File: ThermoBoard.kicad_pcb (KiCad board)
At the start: 4 copper layers, 66 x 75 mm, 153 parts, among them J100 Conn_01x05_Pin, J101 Conn_01x03, J102 TC2030, J103 Screw_Terminal_01x02, J104 USB_C_Receptacle_USB2.0_16P, J200 RJ45_Hanrun_HR911105A_Horizon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, J300 Conn_01x02_Pin, J301 Conn_01x02_Pin, J302 Conn_01x02_Pin, J303 Conn_01x02_Pin, J400 Conn_01x04_Pin, SW100 SW_Push, U100 STM32H563RITx, U101 AP2112K-3.3, U102 USBLC6-2SC6, U200 LAN8742A, U201 USBLC6-4SC6, U300 MAX31856, U301 MAX31856, U302 MAX31856, U303 MAX31856, U400 TJA1042T-3, Y100 16MHz, Y200 25MHz

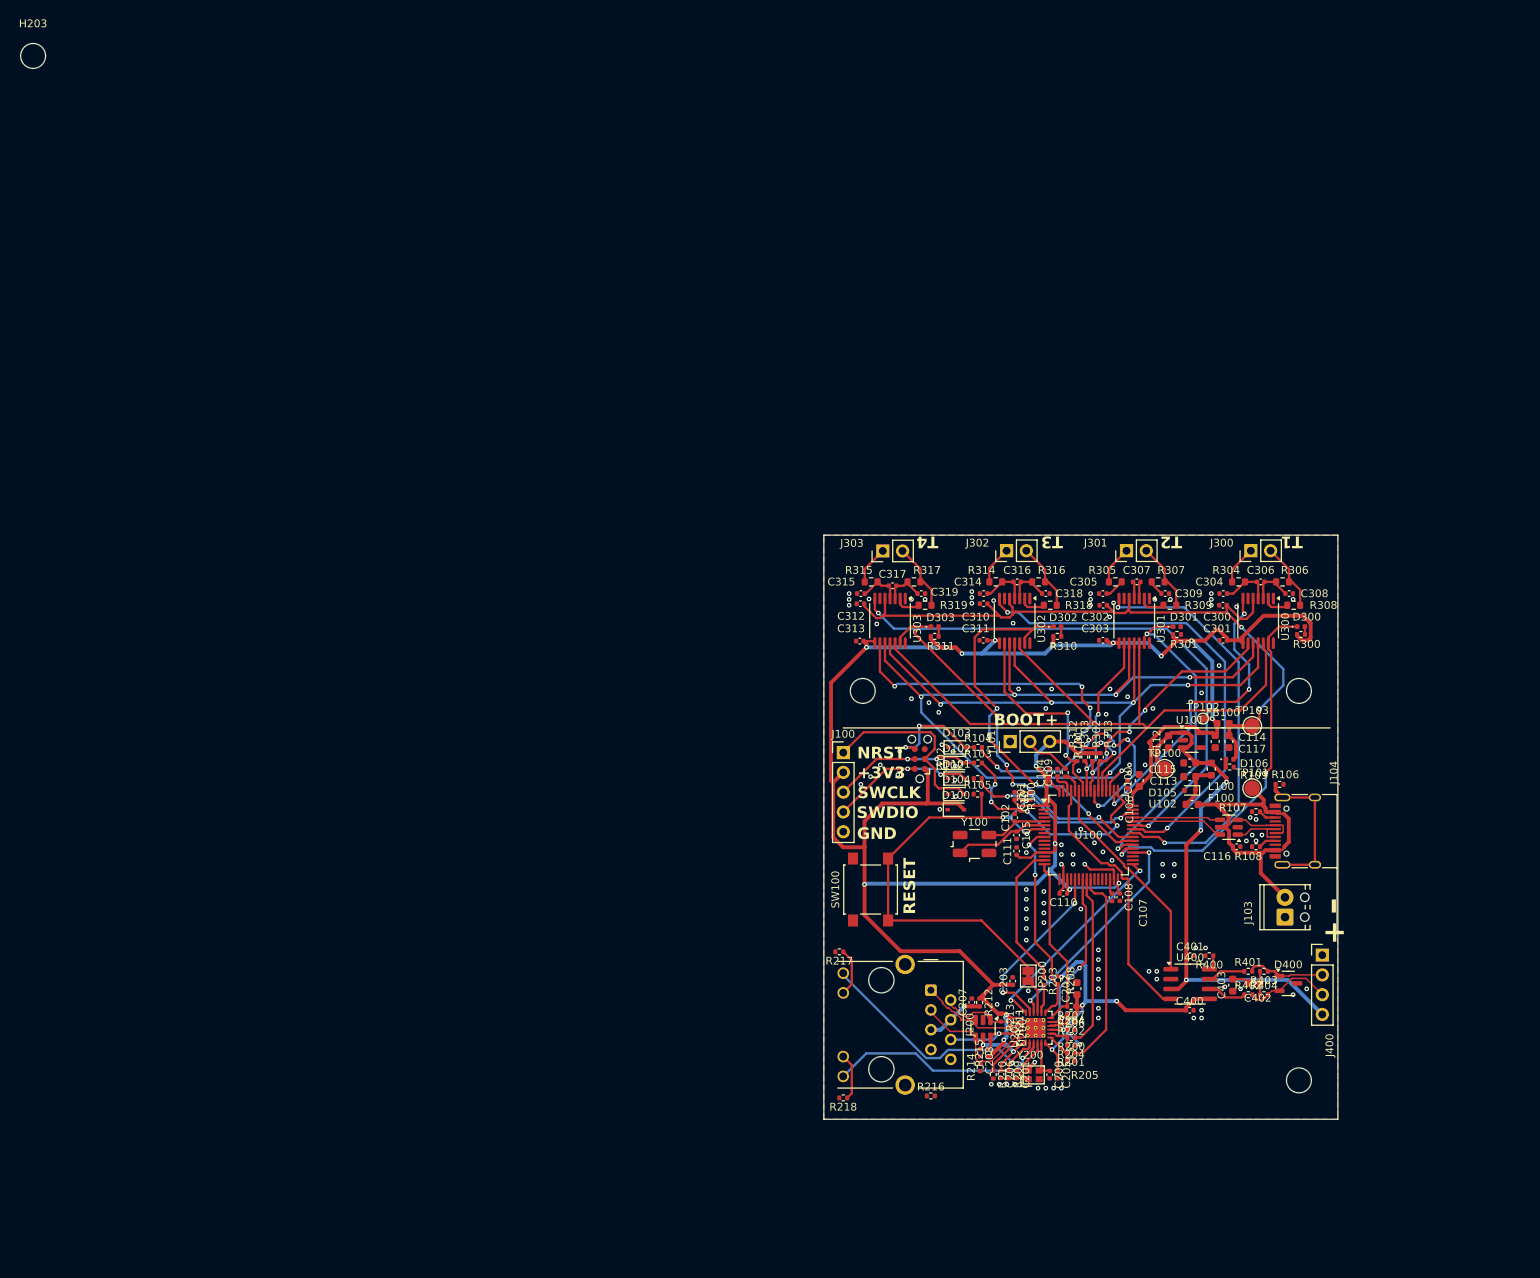
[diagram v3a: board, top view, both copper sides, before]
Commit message: First decent layout
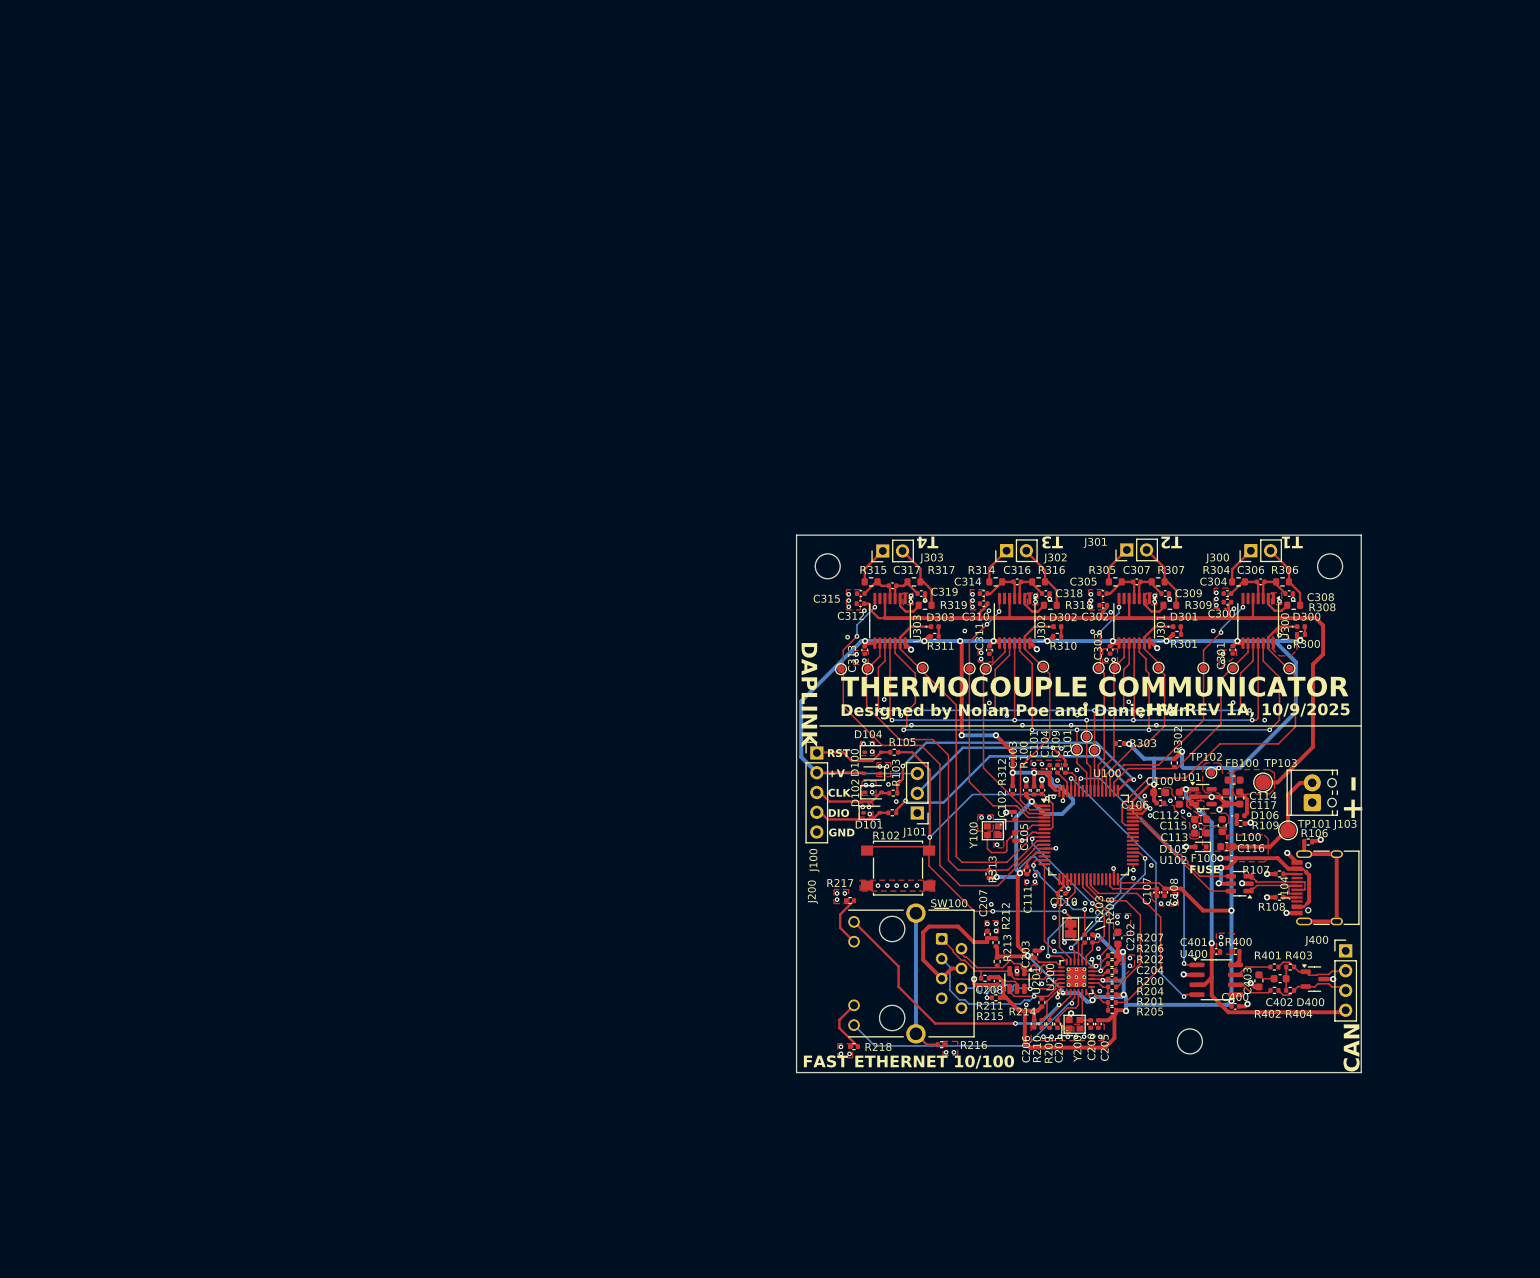
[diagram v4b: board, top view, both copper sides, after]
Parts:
- removed D103: PESD3V3, Diode_SMD:D_SOD-323
- removed H203: MountingHole, MountingHole:MountingHole_3.2mm_M3
- removed J102: TC2030, Connector:Tag-Connect_TC2030-IDC-NL_2x03_P1.27mm_Vertical
- removed R104: 49R9, Resistor_SMD:R_0402_1005Metric
- added TP104: TestPoint_Small, TestPoint:TestPoint_Pad_D1.0mm, F.Cu at (138.7, 90.9)
- added TP105: TestPoint_Small, TestPoint:TestPoint_Pad_D1.0mm, F.Cu at (137.5, 92.5)
- added TP106: TestPoint_Small, TestPoint:TestPoint_Pad_D1.0mm, F.Cu at (153.7, 82.1)
- added TP107: TestPoint_Small, TestPoint:TestPoint_Pad_D1.0mm, F.Cu at (164.8, 82.1)
- added TP108: TestPoint_Small, TestPoint:TestPoint_Pad_D1.0mm, F.Cu at (123.7, 82.1)
- added TP109: TestPoint_Small, TestPoint:TestPoint_Pad_D1.0mm, F.Cu at (133.2, 81.9)
- added TP110: TestPoint_Small, TestPoint:TestPoint_Pad_D1.0mm, F.Cu at (125.8, 82.2)
- added TP114: TestPoint_Small, TestPoint:TestPoint_Pad_D1.0mm, F.Cu at (140.3, 82.1)
- added TP115: TestPoint_Small, TestPoint:TestPoint_Pad_D1.0mm, F.Cu at (148.0, 82.0)
- added TP116: TestPoint_Small, TestPoint:TestPoint_Pad_D1.0mm, F.Cu at (142.4, 82.1)
- added TP120: TestPoint_Small, TestPoint:TestPoint_Pad_D1.0mm, F.Cu at (107.2, 82.2)
- added TP121: TestPoint_Small, TestPoint:TestPoint_Pad_D1.0mm, F.Cu at (117.7, 82.0)
- added TP122: TestPoint_Small, TestPoint:TestPoint_Pad_D1.0mm, F.Cu at (110.6, 82.2)
- added TP300: TestPoint_Small, TestPoint:TestPoint_Pad_D1.0mm, F.Cu at (157.5, 82.1)
- J104: footprint Connector_USB:USB_C_Receptacle_HRO_TYPE-C-31-M-12 -> Library:USB_C_Receptacle_HRO_TYPE-C-31-M-12
- J200: footprint Connector_RJ:RJ45_Hanrun_HR911105A_Horizontal -> Library:RJ45_Hanrun_HR911105A_Horizontal
- TP100: value +5V -> TestPoint_Small; footprint TestPoint:TestPoint_Pad_D2.0mm -> TestPoint:TestPoint_Pad_D1.0mm
- U200: footprint Package_DFN_QFN:VQFN-24-1EP_4x4mm_P0.5mm_EP2.5x2.5mm_ThermalVias -> Library:VQFN-24-1EP_4x4mm_P0.5mm_EP2.5x2.5mm_ThermalVias
- Y100: value 16MHz -> X322516MMB4SI; footprint Crystal:Crystal_SMD_EuroQuartz_MJ-4Pin_5.0x3.2mm -> Library:CRYSTAL-SMD_4P-L2.0-W1.6-BL
- moved R313 20.7 mm to (126.2, 108.5), turned to 90 degrees
- moved H200 16.6 mm to (105.5, 69.0)
- moved H201 16.5 mm to (170.0, 69.0)
- moved J103 15.1 mm to (167.7, 99.3)
- moved J101 15.0 mm to (117.0, 100.7), turned to 180 degrees
- moved H202 14.9 mm to (152.0, 130.0)
- moved D104 12.0 mm to (111.3, 92.9)
- moved R105 12.0 mm to (114.0, 92.9)
- moved R102 11.8 mm to (113.8, 100.7)
- moved D101 11.7 mm to (111.2, 100.7)
- moved D100 11.7 mm to (111.2, 95.6), turned to 180 degrees
- moved R103 11.5 mm to (113.9, 98.1)
- moved R214 11.5 mm to (133.0, 125.0)
- moved D102 11.3 mm to (111.3, 98.0)
- moved R302 10.5 mm to (150.0, 94.2)
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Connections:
- net Net-(D105-K) renamed /Microcontroller/PNET
- TP100 pad 1: +5V -> SPI_SCK
- U100 pad 10: unconnected-(U100-PC2-Pad10) -> SPI_CS4
- U100 pad 11: unconnected-(U100-PC3-Pad11) -> NDRDY4
- U100 pad 2: unconnected-(U100-PC13-Pad2) -> NFAULT3
- U100 pad 3: unconnected-(U100-PC14-Pad3) -> SPI_CS3
- U100 pad 37: NFAULT1 -> unconnected-(U100-PC6-Pad37)
- U100 pad 38: NFAULT2 -> unconnected-(U100-PC7-Pad38)
- U100 pad 39: NFAULT3 -> unconnected-(U100-PC8-Pad39)
- U100 pad 4: unconnected-(U100-PC15-Pad4) -> NDRDY3
- U100 pad 40: NFAULT4 -> unconnected-(U100-PC9-Pad40)
- U100 pad 41: NDRDY2 -> unconnected-(U100-PA8-Pad41)
- U100 pad 42: NDRDY3 -> unconnected-(U100-PA9-Pad42)
- U100 pad 43: NDRDY4 -> NFAULT1
- U100 pad 50: NDRDY1 -> SPI_CS1
- U100 pad 51: SPI_SCK -> NDRDY1
- U100 pad 52: SPI_MISO -> NFAULT2
- U100 pad 53: SPI_MOSI -> SPI_CS2
- U100 pad 54: SPI_CS4 -> NDRDY2
- U100 pad 55: /Microcontroller/SWO -> SPI_SCK
- U100 pad 56: SPI_CS1 -> SPI_MISO
- U100 pad 57: SPI_CS2 -> SPI_MOSI
- U100 pad 58: SPI_CS3 -> unconnected-(U100-PB6-Pad58)
- U100 pad 8: unconnected-(U100-PC0-Pad8) -> NFAULT4
- Y100 pad 1: /Microcontroller/HSE_OUT -> /Microcontroller/HSE_IN
- Y100 pad 3: /Microcontroller/HSE_IN -> /Microcontroller/HSE_OUT
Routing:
- net +3V3: track 357.7 -> 398.8 mm, vias 24 -> 31
- net GND: track 10.7 -> 50.7 mm, vias 113 -> 169
- net /Microcontroller/SWO: track 37.1 -> 0.00 mm, vias 6 -> 0
- net NDRDY2: track 54.4 -> 26.3 mm
- net NDRDY3: track 61.9 -> 36.7 mm
- net NFAULT3: track 51.7 -> 31.7 mm, vias 4 -> 0
- net Net-(J200-PadSH): track 0.00 -> 18.9 mm
- net /Microcontroller/SWDIO: track 22.7 -> 41.3 mm
- net /Microcontroller/JUMPER_BOOT0: track 5.86 -> 22.7 mm, vias 0 -> 1
- net +5V: track 68.2 -> 51.8 mm
- net /Microcontroller/CONN_NRST: track 24.6 -> 9.95 mm
- net /Microcontroller/CONN_SWO: track 13.6 -> 0.00 mm, vias 2 -> 0
- net Net-(J200-RCT): track 7.50 -> 21.0 mm, vias 1 -> 0
- net NFAULT2: track 42.0 -> 28.9 mm, vias 2 -> 0
- net NRST: track 59.4 -> 72.0 mm, vias 3 -> 4
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- added copper zone on F.Cu, net +3.3VA
- added copper zone on F.Cu, net +3V3
- added copper zone on F.Cu, net +5V
- added copper zone on F.Cu, net +VDC
- added copper zone on F.Cu, net /Microcontroller/PNET
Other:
- board size 66 x 75 mm -> 72.5 x 69 mm
- board text added: "+5V ONLY"
- board text added: "+V"
- board text added: "CAN"
- board text added: "CAN+"
- board text added: "CAN-"
- board text added: "CLK"
- board text added: "DAPLINK"
- board text added: "DIO"
- board text added: "Designed by Nolan Poe and Daniel Fan"
- board text added: "FAST ETHERNET 10/100"
- board text added: "FUSE"
- board text added: "HW REV 1A, 10/9/2025"
- board text added: "RST"
- board text added: "THERMOCOUPLE COMMUNICATOR"
- board text removed: "${REFERENCE}"
- board text removed: "+3V3"
- board text removed: "BOOT"
- board text removed: "NRST"
- board text removed: "RESET"
- board text removed: "SWCLK"
- board text removed: "SWDIO"

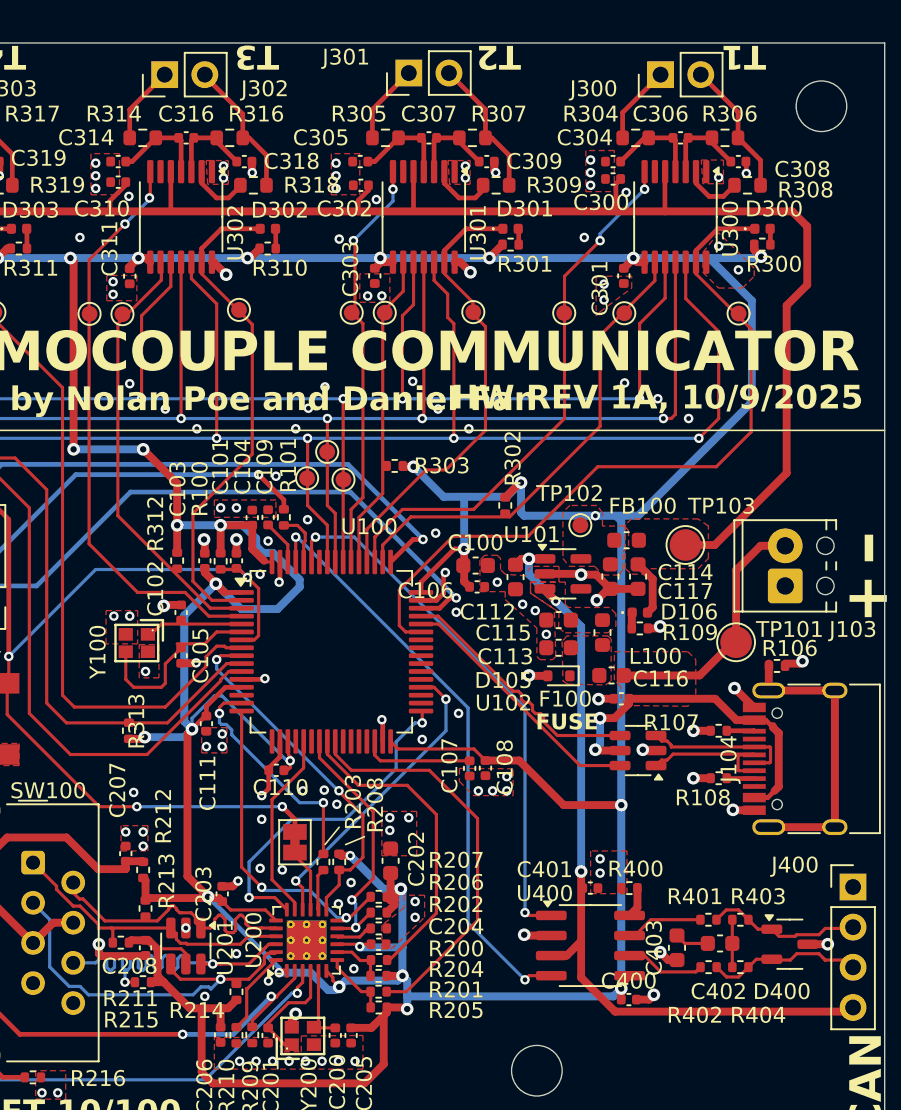
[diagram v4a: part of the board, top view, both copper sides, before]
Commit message: Better plots, make the fuse really obvious
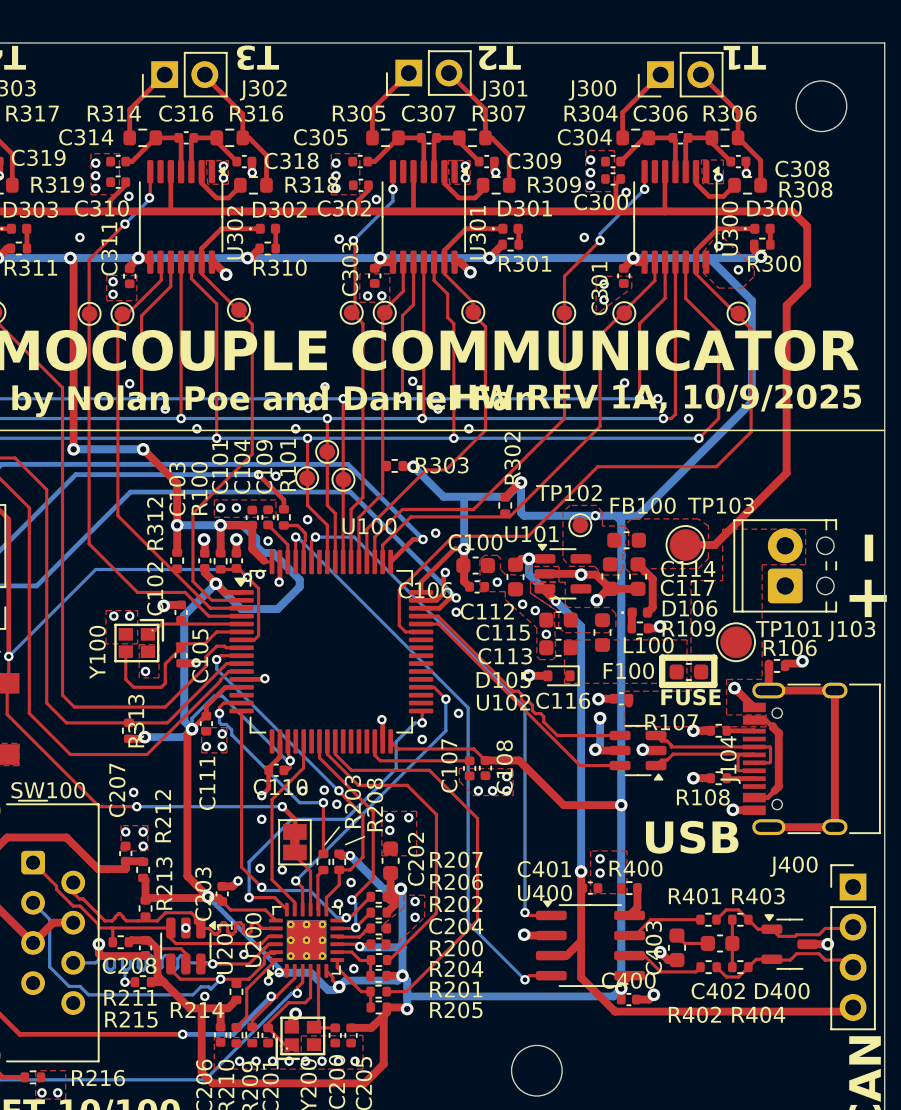
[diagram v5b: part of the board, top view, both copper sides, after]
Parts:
- moved F100 4.89 mm to (161.6, 104.8)
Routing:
- net +VDC: track 38.1 -> 11.3 mm
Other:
- board text added: "USB"

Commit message: Pre-via
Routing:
- net +VDC: track 11.3 -> 14.2 mm
- net GND: vias 169 -> 531
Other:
- board text added: "{ "ViaStitching": "0.2", "stitch_zone_0": { "HSpacing": "1", "VSpacing": "1", "HOffset": "0", "VOffset": "0", "Clearance": "0", "Randomize": false } }"
- board text added: "{ "ViaStitching": "0.2", "stitch_zone_0": { "HSpacing": "2.5", "VSpacing": "2.5", "HOffset": "0", "VOffset": "0", "Clearance": "0", "Randomize": false } }"

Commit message: Actually Pre-via
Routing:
- net GND: vias 531 -> 170

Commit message: Post-stitch
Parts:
- added TP111: +5V, TestPoint:TestPoint_Pad_D1.5mm, F.Cu at (158.8, 104.2)
- TP101: footprint TestPoint:TestPoint_Pad_D2.0mm -> TestPoint:TestPoint_Pad_D1.5mm
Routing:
- net GND: vias 170 -> 401
- added copper zone on B.Cu, net GND
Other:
- board text added: "{ "ViaStitching": "0.2", "stitch_zone_0": { "HSpacing": "2.5", "VSpacing": "2.5", "HOffset": "0", "VOffset": "0", "Clearance": ".3", "Randomize": false } }"
